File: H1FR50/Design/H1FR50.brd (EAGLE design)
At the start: 34.6 x 60 mm, 49 parts, among them P1 HEXABIT_17.32_X2_NO_P5, U1 STM32F091RBT6STMICROELECTRONI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, U2 TPS22943DCKR, U3 BGA824N6, U4 TESEO-LIV3F, U5 B39162B4327P810, X1 XTALL_CSTCE8M00G52

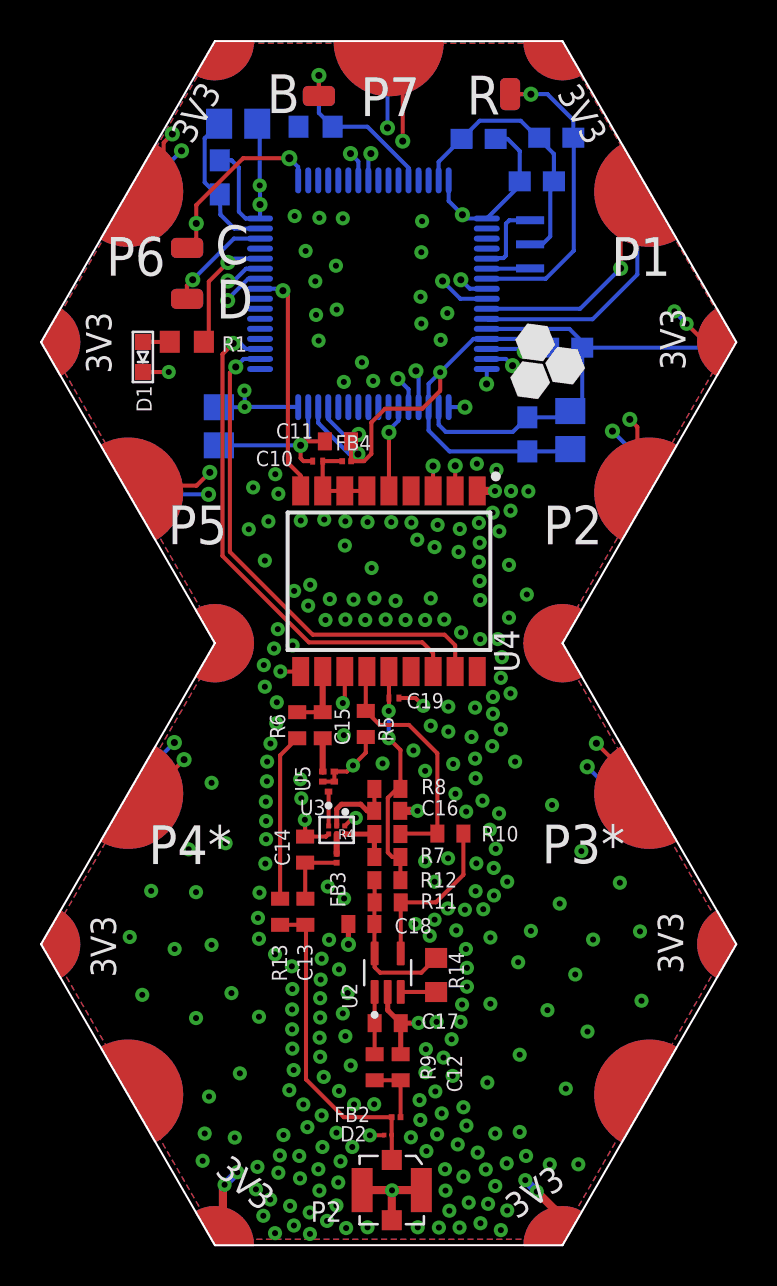
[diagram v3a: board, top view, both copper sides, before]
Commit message: - Changed Polygen for layer 1 to GND - Wrote board specification on documentation layer
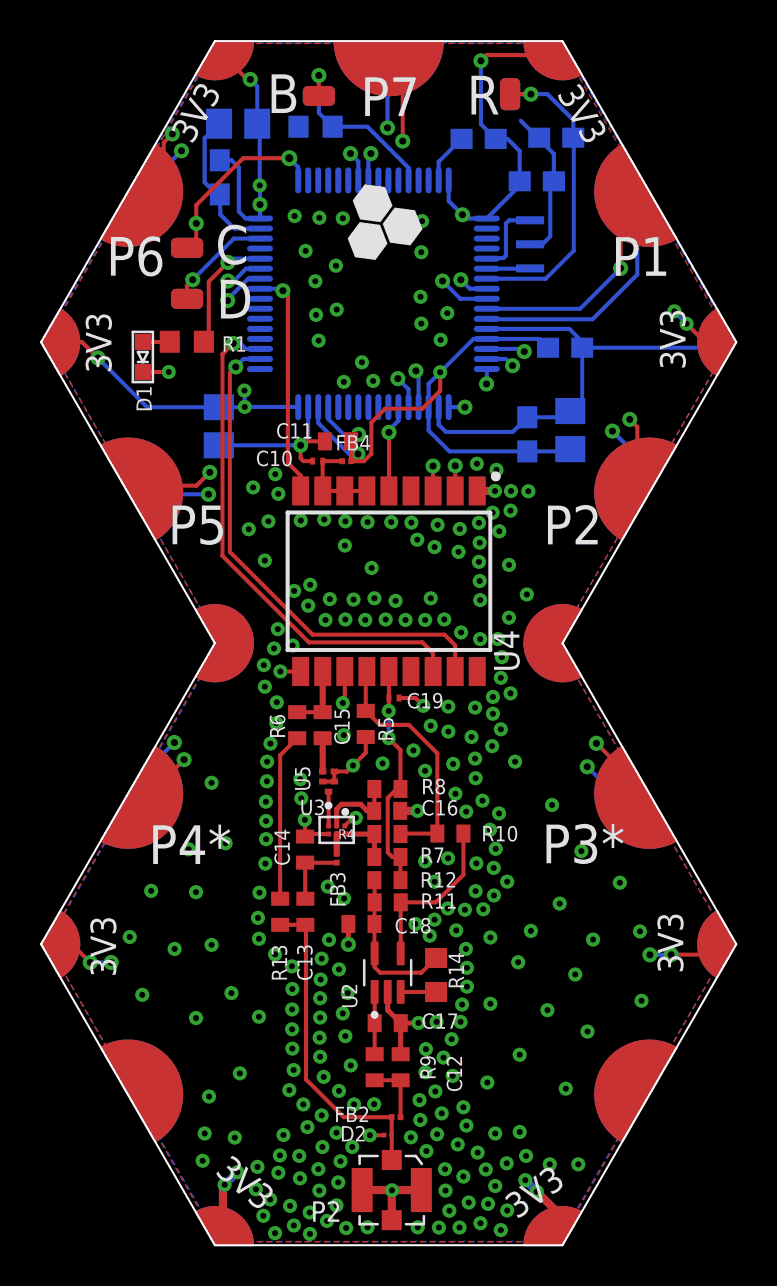
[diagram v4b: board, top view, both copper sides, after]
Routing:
- net VDD: track 58.1 -> 86.5 mm, vias 12 -> 19
- net GND: track 78.7 -> 75.3 mm
- added copper zone on layer 1, net GND
- removed copper zone on layer 1, net VDD
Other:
- board text added: "Total Thickness 1.6 mm --------------------------------------------------------- copper_top_l1.gbr : Top Conductor - Copper: Thickness 0.035 mm Dielectric - FR-4: Thickness 0.175 mm copper_inner_l2.gbr : GND Plane - Copper: Thickness 0.035 mm Dielectric - FR-4: Thickness 1.11 mm copper_inner_l3.gbr : VDD Plane - Copper: Thickness 0.035 mm Dielectric - FR-4: Thickness 0.175 mm copper_bottom_l4.gbr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"

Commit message: Removed all Blined Vias..
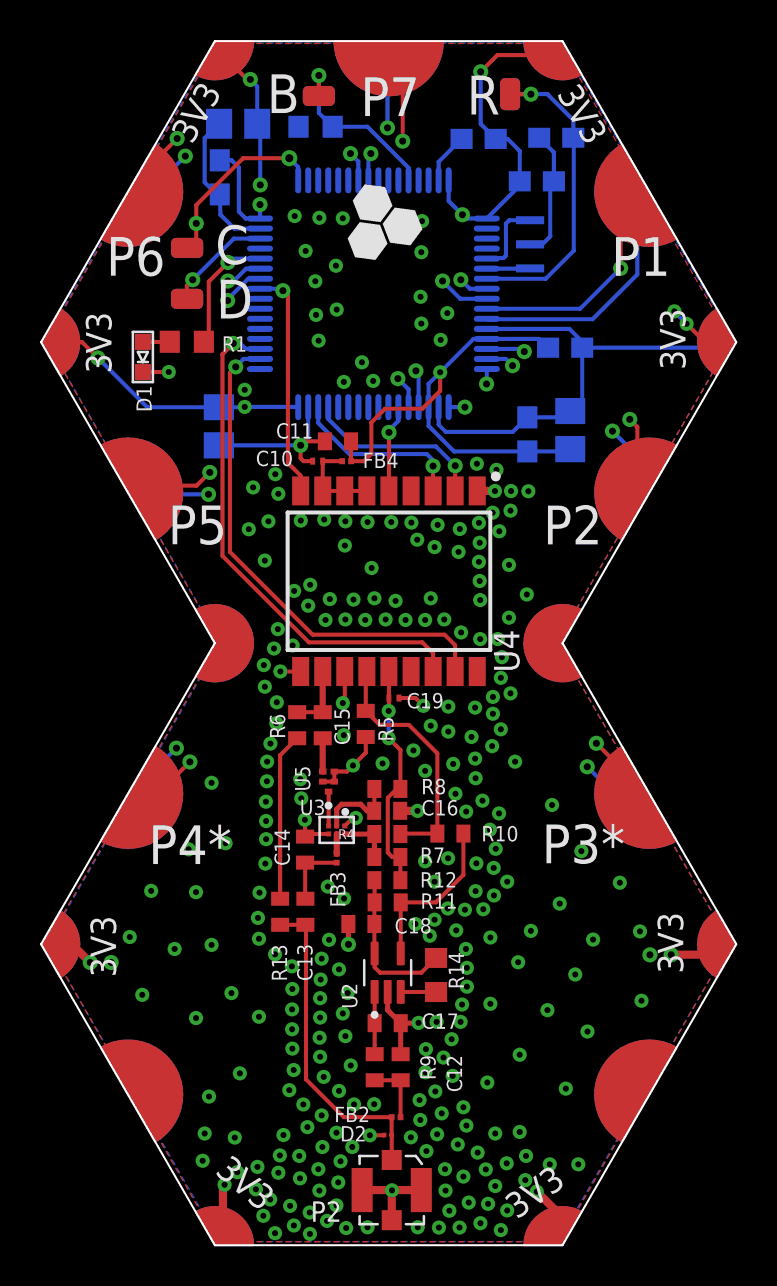
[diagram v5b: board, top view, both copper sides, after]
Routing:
- net GND: track 75.3 -> 74.0 mm
- net VDD: track 86.5 -> 87.1 mm
- net UART1_RX*: track 31.7 -> 31.1 mm
- net UART3_RX: track 8.68 -> 8.81 mm, vias 2 -> 1
- net UART3_TX: vias 2 -> 1

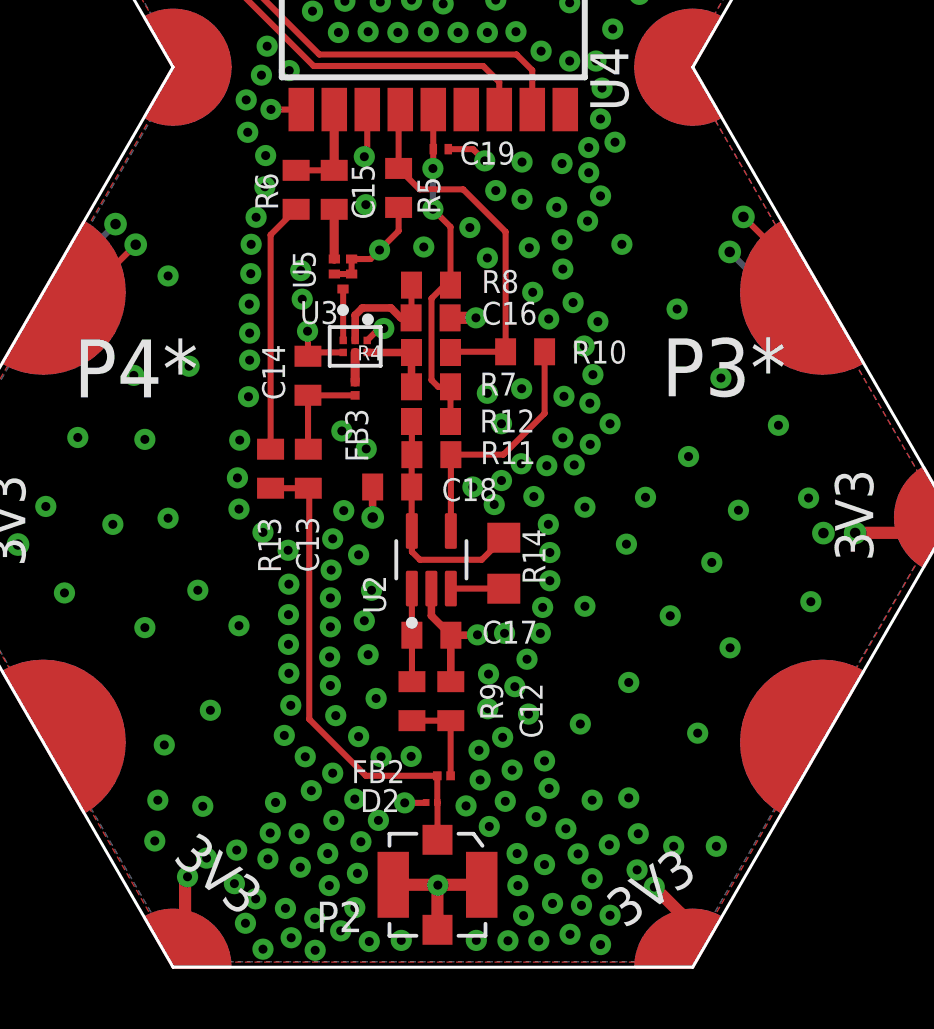
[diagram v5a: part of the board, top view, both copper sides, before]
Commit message: - Changed RF Connector.. - Documents and BOM were updated..
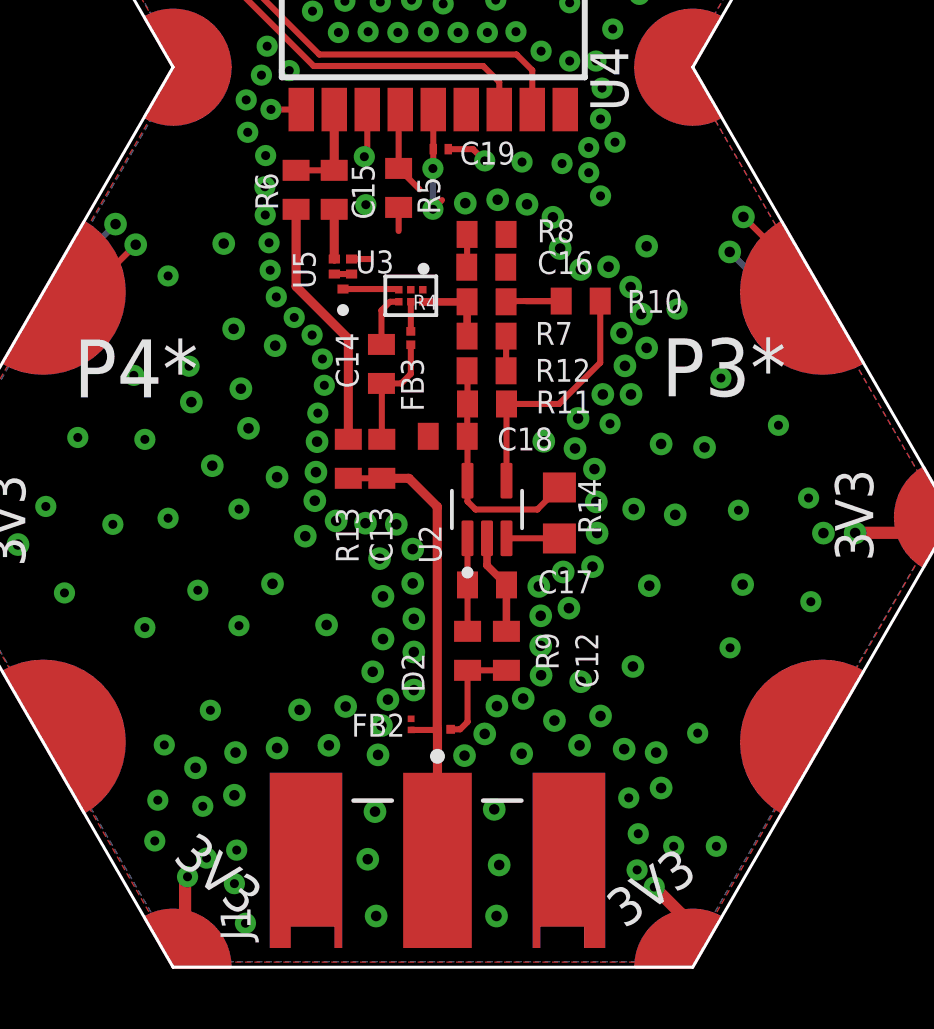
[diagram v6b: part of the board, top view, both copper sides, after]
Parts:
- removed P2: (no value), HEXABITZ_CONNECTION_PARTS:0734120110
- added J1: MOLEX_INC_0732511150MOLEX_INC_0732511150_0_0, HEXABITZ_CONNECTION_PARTS:MOLEX_INC_0732511150_0
- moved D2 2.69 mm to (-0.72, -36.9), turned to 270 degrees
- moved R13 2.61 mm to (-2.82, -28.1)
- moved C16 2.51 mm to (1.78, -21.7)
- moved C18 2.51 mm to (0.50, -27.3)
- moved FB3 2.51 mm to (-0.74, -24.0)
- moved R10 2.51 mm to (4.93, -22.8)
- moved R11 2.51 mm to (1.80, -26.2)
- moved R12 2.51 mm to (1.79, -25.1)
- moved R4 2.51 mm to (1.79, -22.8)
- moved R7 2.51 mm to (1.79, -24.0)
- moved R8 2.51 mm to (1.79, -20.6)
- moved U3 2.51 mm to (-0.74, -22.6)
- moved C12 2.50 mm to (2.45, -34.5)
- moved R14 2.50 mm to (4.22, -29.9)
- moved R9 2.50 mm to (1.16, -34.5)
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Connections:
- net GND: now also J1.2, J1.3, J1.4, J1.5; no longer P2.2, P2.3, P2.4
- net N$3: now also J1.1; no longer P2.1
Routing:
- net GND: track 74.0 -> 63.3 mm, vias 274 -> 224
- net VCC_RF: track 11.5 -> 5.20 mm
- net ANTOFF: track 12.3 -> 6.02 mm
- net N$19: track 4.04 -> 1.10 mm
- net N$1: track 3.38 -> 3.95 mm
- net N$11: track 3.14 -> 3.69 mm

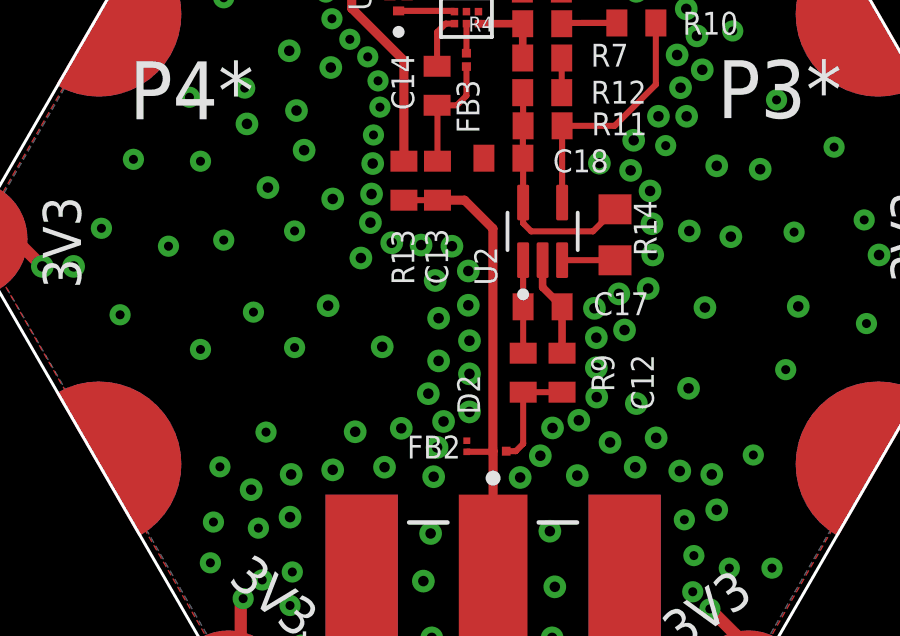
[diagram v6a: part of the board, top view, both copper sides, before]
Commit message: - Changed the RF route width to 10 mil
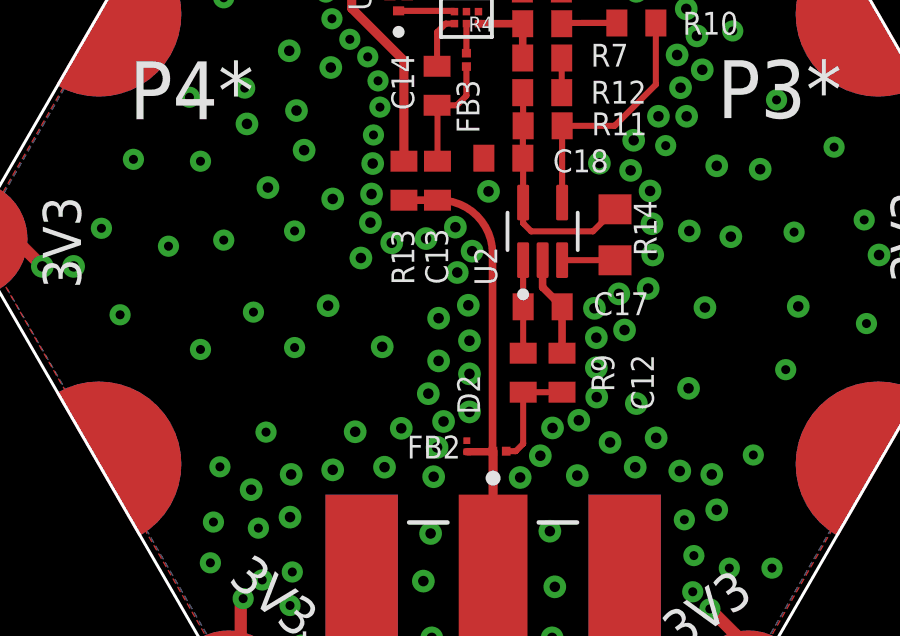
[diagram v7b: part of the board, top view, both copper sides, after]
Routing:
- net GND: vias 224 -> 225
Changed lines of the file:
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@@
 <contactref element="R13" pad="2"/>
 <contactref element="J1" pad="1"/>
-<wire x1="-2.8194" y1="-28.7043" x2="-1.7018" y2="-28.7043" width="0.2032" layer="1"/>
+<wire x1="-2.8194" y1="-28.7043" x2="-1.7018" y2="-28.7043" width="0.254" layer="1"/>
 <wire x1="0.1524" y1="-41.4397" x2="0.1524" y2="-37.0774" width="0.3048" layer="1"/>
 <wire x1="0.1524" y1="-37.0774" x2="0.1463" y2="-37.0713" width="0.2032" layer="1"/>
 <wire x1="0.1463" y1="-37.0713" x2="0.1264" y2="-37.0912" width="0.2032" layer="1"/>
-<wire x1="0.1264" y1="-37.0912" x2="-0.7239" y2="-37.0912" width="0.2032" layer="1"/>
-<wire x1="0.1463" y1="-37.0713" x2="0.1463" y2="-29.6507" width="0.3048" layer="1"/>
-<wire x1="0.1463" y1="-29.6507" x2="-0.8001" y2="-28.7043" width="0.3048" layer="1"/>
-<wire x1="-0.8001" y1="-28.7043" x2="-1.7018" y2="-28.7043" width="0.3048" layer="1"/>
+<wire x1="0.1264" y1="-37.0912" x2="-0.7239" y2="-37.0912" width="0.254" layer="1"/>
+<wire x1="0.1336" y1="-30.4762" x2="0.1336" y2="-37.0332" width="0.254" layer="1"/>
+<wire x1="0.1463" y1="-37.0713" x2="0.1463" y2="-37.0459" width="0.254" layer="1"/>
+<wire x1="0.1463" y1="-37.0459" x2="0.1336" y2="-37.0332" width="0.254" layer="1"/>
+<wire x1="-1.6383" y1="-28.7043" x2="-1.7018" y2="-28.7043" width="0.254" layer="1"/>
+<wire x1="0.1336" y1="-30.4762" x2="-1.6383" y2="-28.7043" width="0.254" layer="1" curve="90"/>
 </signal>
 <signal name="RF_IN">
@@
 <via x="5.4483" y="-29.4894" extent="1-16" drill="0.35"/>
 <via x="6.6929" y="-29.7307" extent="1-16" drill="0.35"/>
-<via x="-1.2192" y="-30.2387" extent="1-16" drill="0.35"/>
-<via x="-2.2479" y="-30.2006" extent="1-16" drill="0.35"/>
+<via x="-1.1049" y="-29.6037" extent="1-16" drill="0.35"/>
+<via x="-2.0828" y="-29.9847" extent="1-16" drill="0.35"/>
 <via x="-3.2258" y="-30.1244" extent="1-16" drill="0.35"/>
 <via x="-3.937" y="-29.4513" extent="1-16" drill="0.35"/>
@@
 <via x="-5.3467" y="-32.2199" extent="1-16" drill="0.35"/>
 <via x="-3.5433" y="-33.5915" extent="1-16" drill="0.35"/>
-<via x="-1.778" y="-31.3817" extent="1-16" drill="0.35"/>
-<via x="-0.6731" y="-31.0642" extent="1-16" drill="0.35"/>
+<via x="-1.0414" y="-31.115" extent="1-16" drill="0.35"/>
+<via x="-0.5461" y="-30.4038" extent="1-16" drill="0.35"/>
 <via x="-1.6637" y="-32.639" extent="1-16" drill="0.35"/>
 <via x="-0.6731" y="-32.2072" extent="1-16" drill="0.35"/>
@@
 <via x="10.3251" y="-32.2453" extent="1-16" drill="0.35"/>
 <via x="9.0551" y="-27.6733" extent="1-16" drill="0.35"/>
+<via x="0" y="-28.4099" extent="1-16" drill="0.35"/>
 </signal>
 <signal name="VDD3">

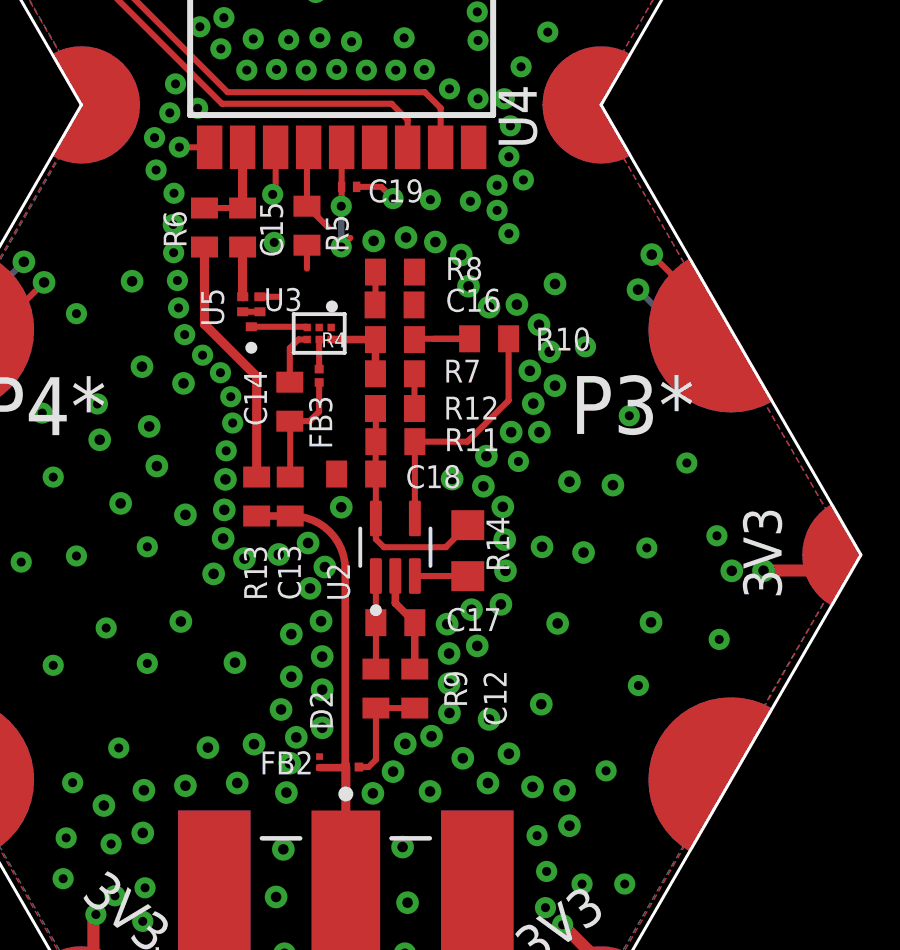
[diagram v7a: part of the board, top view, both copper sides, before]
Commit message: - Fixed some DRC errors.. - Changed TOP layer (1) polygon isolation to 7 mill
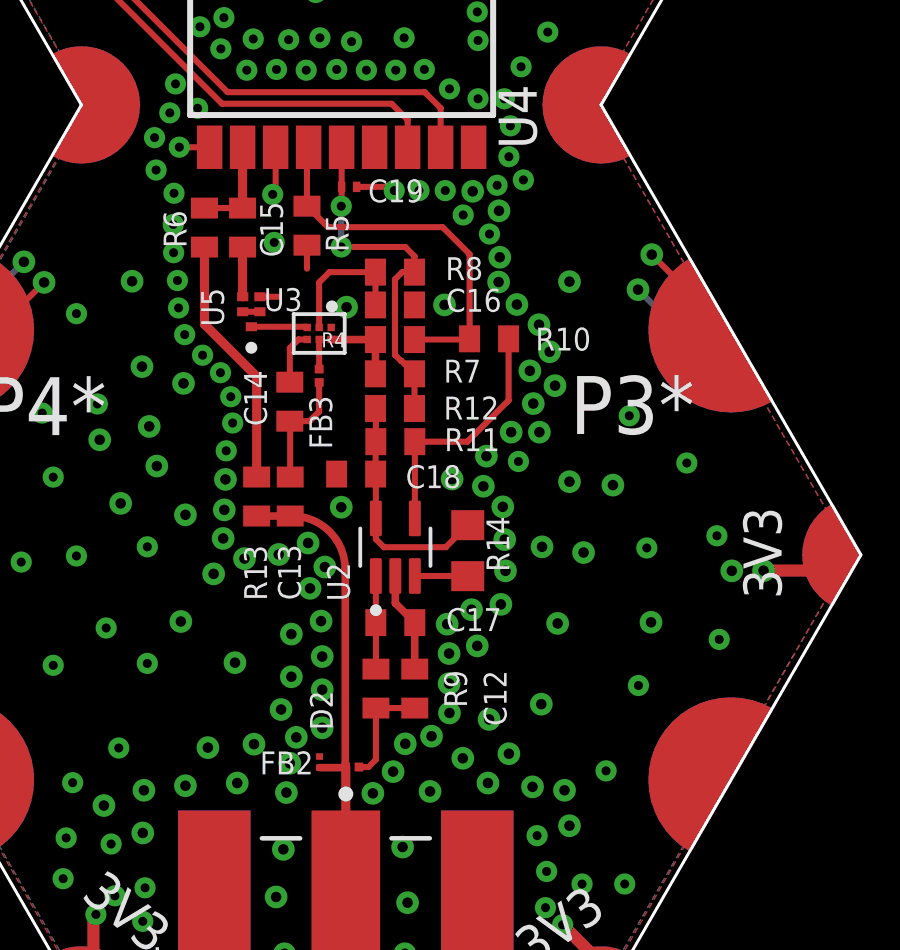
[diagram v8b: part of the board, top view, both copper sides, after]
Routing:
- net ANTOFF: track 6.02 -> 12.8 mm
- net VCC_RF: track 5.20 -> 11.8 mm
- net N$19: track 1.10 -> 4.61 mm
- net GND: track 63.3 -> 63.2 mm, vias 225 -> 224
